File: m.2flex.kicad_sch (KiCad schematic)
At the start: 2 parts, among them CN8 DF40C-20DP-0.4V, CN9 DF40C-20DP-0.4V

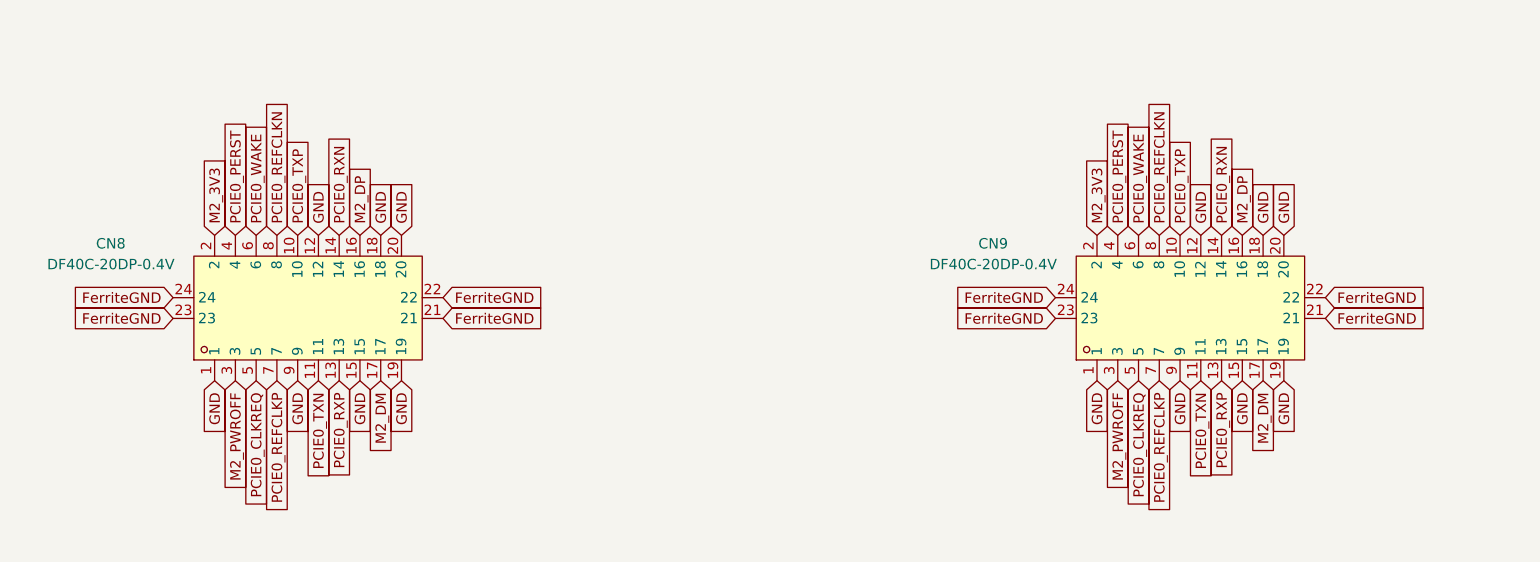
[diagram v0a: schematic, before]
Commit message: finished radio board with load switches and flash, fixed b2b connector, started antenna module and rf sense switching circuit
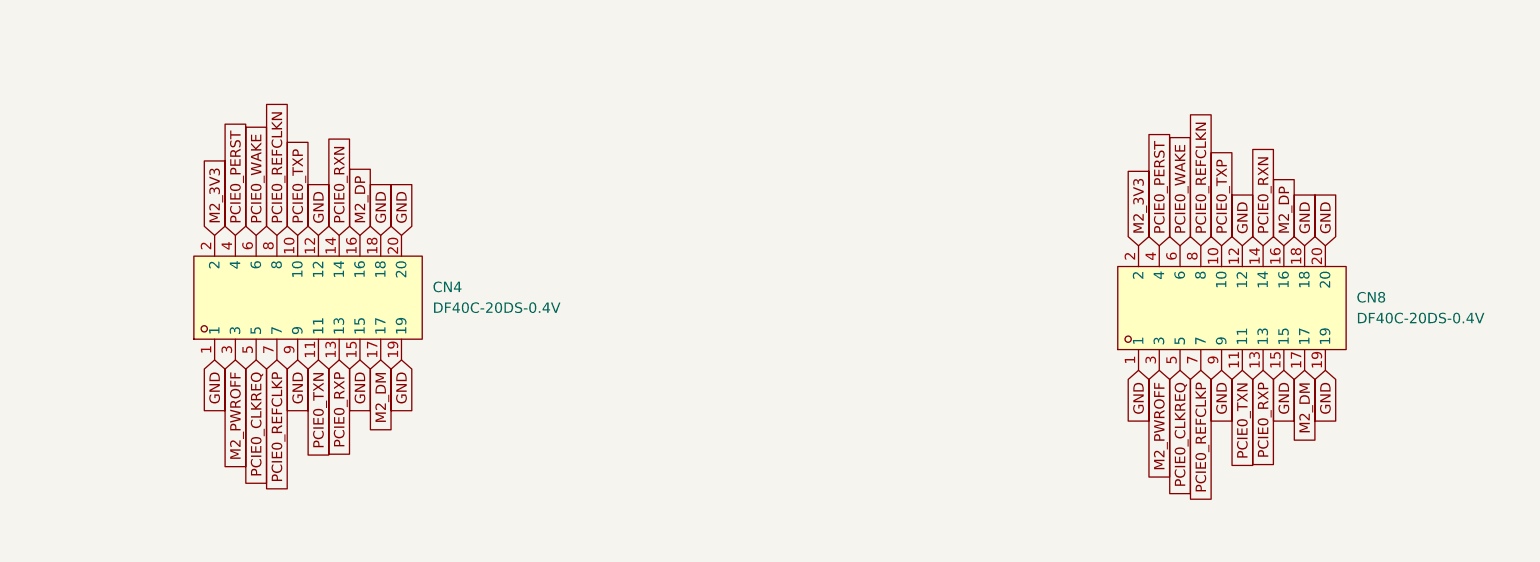
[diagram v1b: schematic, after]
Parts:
- removed CN8, CN9: DF40C-20DP-0.4V, slate113:CONN-SMD_20P-P0.40_HRS_DF40TC-20DP-0.4V, symbol slate113:DF40C-20DP-0.4V
- added CN4, CN8: DF40C-20DS-0.4V, slate113:CONN-SMD_20P-P0.40_DF40C-20DS-0.4V, symbol slate113:DF40C-20DS-0.4V
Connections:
- net GND: now also CN4.1, CN4.12, CN4.15, CN4.18, CN4.19, CN4.20, CN4.9, CN8.1, CN8.12, CN8.15, CN8.18, CN8.19, CN8.20, CN8.9
- net M2_3V3: now also CN4.2, CN8.2
- net M2_DM: now also CN4.17, CN8.17
- net M2_DP: now also CN4.16, CN8.16
- net M2_PWROFF: now also CN4.3, CN8.3
- net PCIE0_CLKREQ: now also CN4.5, CN8.5
- net PCIE0_PERST: now also CN4.4, CN8.4
- net PCIE0_REFCLKN: now also CN4.8, CN8.8
- net PCIE0_REFCLKP: now also CN4.7, CN8.7
- net PCIE0_RXN: now also CN4.14, CN8.14
- net PCIE0_RXP: now also CN4.13, CN8.13
- net PCIE0_TXN: now also CN4.11, CN8.11
- net PCIE0_TXP: now also CN4.10, CN8.10
- net PCIE0_WAKE: now also CN4.6, CN8.6

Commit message: finished rf sense and io board closure, added audio system with pcm and three spdt switches, made changes tp lte module, added ldo and sd/sim slot, updated m.2/audio schematics, added new mic msop qfn sot footprints, and added a protection system for non EM06-A Cards
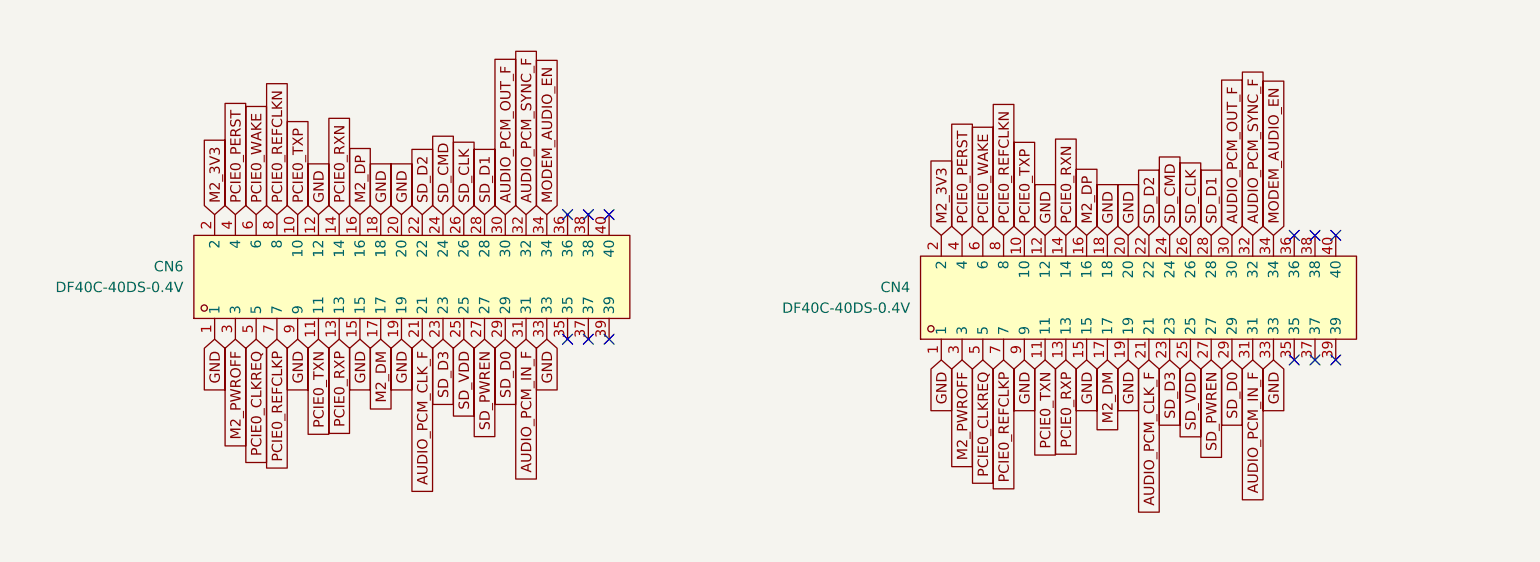
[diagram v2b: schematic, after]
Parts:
- removed CN4, CN8: DF40C-20DS-0.4V, slate113:CONN-SMD_20P-P0.40_DF40C-20DS-0.4V, symbol slate113:DF40C-20DS-0.4V
- added CN4, CN6: DF40C-40DS-0.4V, slate113:CONN-SMD_DF40C-40DS-0.4V51, symbol slate113:DF40C-40DS-0.4V
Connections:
- net GND: now also CN4.1, CN4.12, CN4.15, CN4.18, CN4.19, CN4.20, CN4.33, CN4.9, CN6.1, CN6.12, CN6.15, CN6.18, CN6.19, CN6.20, CN6.33, CN6.9
- net M2_3V3: now also CN4.2, CN6.2
- net M2_DM: now also CN4.17, CN6.17
- net M2_DP: now also CN4.16, CN6.16
- net M2_PWROFF: now also CN4.3, CN6.3
- net PCIE0_CLKREQ: now also CN4.5, CN6.5
- net PCIE0_PERST: now also CN4.4, CN6.4
- net PCIE0_REFCLKN: now also CN4.8, CN6.8
- net PCIE0_REFCLKP: now also CN4.7, CN6.7
- net PCIE0_RXN: now also CN4.14, CN6.14
- net PCIE0_RXP: now also CN4.13, CN6.13
- net PCIE0_TXN: now also CN4.11, CN6.11
- net PCIE0_TXP: now also CN4.10, CN6.10
- net PCIE0_WAKE: now also CN4.6, CN6.6
- new net AUDIO_PCM_CLK_F: CN4.21, CN6.21
- new net AUDIO_PCM_IN_F: CN4.31, CN6.31
- new net AUDIO_PCM_OUT_F: CN4.30, CN6.30
- new net AUDIO_PCM_SYNC_F: CN4.32, CN6.32
- new net MODEM_AUDIO_EN: CN4.34, CN6.34
- new net SD_CLK: CN4.26, CN6.26
- new net SD_CMD: CN4.24, CN6.24
- new net SD_D0: CN4.29, CN6.29
- new net SD_D1: CN4.28, CN6.28
- new net SD_D2: CN4.22, CN6.22
- new net SD_D3: CN4.23, CN6.23
- new net SD_PWREN: CN4.27, CN6.27
- new net SD_VDD: CN4.25, CN6.25
- no-connect marks 0 -> 12
